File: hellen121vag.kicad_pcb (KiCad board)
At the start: 4 copper layers, 164 x 118 mm, 129 parts, among them J1 USB_B_Mini, J10 AudioJack_THR, J2 Conn_01x01, J3 Conn_01x01, J4 Conn_01x01, J5 Conn_01x01, J6 Conn_01x01, J7 Conn_01x08, J8 Conn_01x06, M1 Module-can-0.1, M10 Module-can-0.1, M11 Module-vr-discrete-0.1, M2 Module-power5-0.2, M3 Module-mcu-0.7, M4 Module-input-0.1, M5 Module-knock-0.1, M6 Module-output-0.3, M7 Module-ign8-0.2, M8 Module-power12-0.2, M9 Module-wbo-0.3, P1 368255-2, P10 Pad, P11 Pad, P12 Pad, P13 Pad, P14 Pad, P15 Pad, P16 Pad, P17 Pad, P2 Pad, P20 Pad, P28 Pad, P3 Pad, P4 Pad, P40 Pad, P41 Pad, P43 Pad, P44 Pad, P45 Pad, P46 Pad, P48 Pad, P49 Pad, P5 Pad, P56 Pad, P6 Pad, P61 Pad, P63 Pad, P64 Pad, P66 Pad, P67 Pad, P68 Pad, P69 Pad, P7 Pad, P74 Pad, P8 Pad, P80 Pad, P9 Pad, U1 L6205PD, U2 LPS25HB, U3 MCP6002-xSN, U4 TLS115_SOIC, U5 TLS115_SON

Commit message: Se agrego by avelito
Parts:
- moved U5 35.0 mm to (57.3, 68.4)
- moved C18 35.0 mm to (61.7, 69.0)
- moved C19 35.0 mm to (61.7, 67.1)
- moved U4 35.0 mm to (56.5, 62.8)
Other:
- board text added: "By Abelito"

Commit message: se modifico esquema y pcb
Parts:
- removed D10, D11, D12, D13, D14: B5819W, Diode_SMD:D_SOD-123
- removed D7, D8: LED-GREEN-0805, hellen-one-common:LED-0805
- removed D9: 1N4148WS, hellen-one-common:SOD-323
- removed G***, G6: LOGO, hellen-one-common:LOGO
- removed G3, G5: PROTO_AREA, hellen-one-common:PROTO_AREA
- removed G7: LOGO, rusefi_lib:LOGO
- removed J1: USB_B_Mini, hellen-one-common:USB-MINI-B-VERTICAL
- removed J10: AudioJack_THR, hellen-one-common:Jack_3.5mm_PJ-3250-5A
- removed J2, J3, J4, J5, J6: Conn_01x01, TestPoint:TestPoint_Pad_D2.0mm
- removed J7: Conn_01x08, Connector_PinHeader_2.54mm:PinHeader_1x08_P2.54mm_Vertical
- removed J8: Conn_01x06, Connector_PinHeader_2.54mm:PinHeader_1x06_P2.54mm_Vertical
- removed M10: Module-can-0.1, hellen-one-can-0.1:can
- removed M11: Module-vr-discrete-0.1, hellen-one-vr-discrete-0.1:vr-discrete
- removed M8: Module-power12-0.2, hellen-one-power12-0.2:power12
- removed M9: Module-wbo-0.3, hellen-one-wbo-0.3:wbo
- removed P14, P15, P16, P17, P20, P28, P40, P41, P43, P44, P45, P46, P48, P49, P56, P61, P63, P64, P66, P67, P68, P69, P74, P80: Pad, hellen-one-common:PAD-TH
- removed S1, S2: Button_SPST, hellen-one-common:SMD-2_2.9x3.9x1.7
- added C20: 10u, hellen-one-common:C0805, F.Cu at (159.9, 187.8)
- added C21: 10u, hellen-one-common:C0805, F.Cu at (159.9, 190.1)
- added C22: 10u, hellen-one-common:C0805, F.Cu at (159.9, 192.3)
- added C23: 10u, hellen-one-common:C0805, F.Cu at (159.9, 194.6)
- added C24: 10u, hellen-one-common:C0805, F.Cu at (159.9, 196.8)
- added C25: 100n, hellen-one-common:C0603, F.Cu at (217.2, 170.4)
- added C26: 10n, hellen-one-common:C0603, F.Cu at (220.7, 162.6)
- added C27: 10n, hellen-one-common:C0603, F.Cu at (220.7, 164.5)
- added C28: 100n, hellen-one-common:C0603, F.Cu at (220.7, 166.5)
- added C29: 10n, hellen-one-common:C0603, F.Cu at (220.7, 168.4)
- added C30: 100n, hellen-one-common:C0603, F.Cu at (220.7, 170.4)
- added C31: 10n, hellen-one-common:C0603, F.Cu at (224.1, 162.6)
- added C32: 100n, hellen-one-common:C0603, F.Cu at (224.1, 164.5)
- added C33: 1u, hellen-one-common:C0603, F.Cu at (224.1, 166.5)
- added F10: 50mA, Fuse:Fuse_0603_1608Metric, F.Cu at (217.9, 226.5)
- added F3: 12H1500D, hellen-one-common:PAD-1206-PAD, F.Cu at (219.9, 240.6)
- added F4: 12H1500D, hellen-one-common:PAD-1206-PAD, F.Cu at (219.9, 243.7)
- added F5: 50mA, Fuse:Fuse_0603_1608Metric, F.Cu at (217.9, 214.0)
- added F6: 50mA, Fuse:Fuse_0603_1608Metric, F.Cu at (217.9, 216.5)
- added F7: 50mA, Fuse:Fuse_0603_1608Metric, F.Cu at (217.9, 219.0)
- added F8: 50mA, Fuse:Fuse_0603_1608Metric, F.Cu at (217.9, 221.5)
- added F9: 50mA, Fuse:Fuse_0603_1608Metric, F.Cu at (217.9, 224.0)
- added H1: M3, MountingHole:MountingHole_3.2mm_M3_Pad_Via, F.Cu at (211.9, 216.7)
- added H2: M3, MountingHole:MountingHole_3.2mm_M3_Pad_Via, F.Cu at (211.9, 224.6)
- added H3: M3, MountingHole:MountingHole_3.2mm_M3_Pad_Via, F.Cu at (211.9, 232.6)
- added H4: M3, MountingHole:MountingHole_3.2mm_M3_Pad_Via, F.Cu at (211.9, 240.5)
- added J17: Conn_01x06, Connector_PinHeader_2.54mm:PinHeader_1x06_P2.54mm_Vertical, F.Cu at (222.2, 215.0)
- added J21: Conn_01x05_Male, Connector_Molex:Molex_SPOX_5267-05A_1x05_P2.50mm_Vertical, F.Cu at (149.4, 202.1)
- added J22: USB_B_Mini, hellen-one-common:USB-MINI-B-VERTICAL, F.Cu at (220.4, 189.2)
- added J23: USB_C, kicad6-libraries:USB_C, F.Cu at (219.8, 154.7)
- added L1: 470R@100MHz, Inductor_SMD:L_0603_1608Metric, F.Cu at (217.9, 229.0)
- added L2: 470R@100MHz, Inductor_SMD:L_0603_1608Metric, F.Cu at (217.9, 231.5)
- added Q1: ISL9V3040D3ST, Package_TO_SOT_SMD:TO-252-2, F.Cu at (168.9, 154.7)
- added Q2: ISL9V3040D3ST, Package_TO_SOT_SMD:TO-252-2, F.Cu at (177.1, 154.7)
- added Q3: ISL9V3040D3ST, Package_TO_SOT_SMD:TO-252-2, F.Cu at (185.3, 154.7)
- added Q4: ISL9V3040D3ST, Package_TO_SOT_SMD:TO-252-2, F.Cu at (193.5, 154.7)
- added Q5: ISL9V3040D3ST, Package_TO_SOT_SMD:TO-252-2, F.Cu at (201.7, 154.7)
- added Q6: ISL9V3040D3ST, Package_TO_SOT_SMD:TO-252-2, F.Cu at (209.9, 154.7)
- added R14: 5.6k, hellen-one-common:R0603, F.Cu at (174.8, 239.2)
- added R15: 4.7k, hellen-one-common:R0603, F.Cu at (178.1, 227.5)
- added R24: 4.7k, hellen-one-common:R0603, F.Cu at (181.4, 231.4)
- added R25: 4.7k, hellen-one-common:R0603, F.Cu at (181.4, 233.4)
- added R26: 4.7k, hellen-one-common:R0603, F.Cu at (181.4, 235.3)
- added R27: 4.7k, hellen-one-common:R0603, F.Cu at (181.4, 237.3)
- added R28: 4.7k, hellen-one-common:R0603, F.Cu at (181.4, 239.2)
- added R29: 22, hellen-one-common:R0603, F.Cu at (184.7, 227.5)
- added R30: 22, hellen-one-common:R0603, F.Cu at (184.7, 229.5)
- added R31: 22, hellen-one-common:R0603, F.Cu at (184.7, 231.4)
- added R32: 0, Resistor_SMD:R_2512_6332Metric, F.Cu at (133.8, 211.3)
- added R33: 0, Resistor_SMD:R_2512_6332Metric, F.Cu at (133.8, 216.2)
- added R34: 0, Resistor_SMD:R_2512_6332Metric, F.Cu at (133.8, 221.0)
- added R35: 22, hellen-one-common:R0603, F.Cu at (184.7, 233.4)
- added R36: 22, hellen-one-common:R0603, F.Cu at (184.7, 235.3)
- added R37: 22, hellen-one-common:R0603, F.Cu at (184.7, 237.3)
- added R38: 0, Resistor_SMD:R_2512_6332Metric, F.Cu at (133.8, 225.9)
- added R39: 0, Resistor_SMD:R_2512_6332Metric, F.Cu at (133.8, 230.8)
- added R40: 0, Resistor_SMD:R_2512_6332Metric, F.Cu at (133.8, 235.7)
- added U10: MPX4/MPXH6400_MAP, kicad6-libraries:MPX-4_MAP, F.Cu at (200.8, 170.6)
- added U11: MAX31855KASA, Package_SO:SOIC-8_3.9x4.9mm_P1.27mm, F.Cu at (169.0, 240.2)
- added U6: TLE9201SG, Package_SO:Infineon_PG-DSO-12-11, F.Cu at (144.8, 229.2)
- added U7: TLE9201SG, Package_SO:Infineon_PG-DSO-12-11, F.Cu at (144.8, 238.9)
- added U8: VNLD5160TR-E, Package_SO:SOIC-8_3.9x4.9mm_P1.27mm, F.Cu at (169.0, 227.0)
- added U9: VNLD5160TR-E, Package_SO:SOIC-8_3.9x4.9mm_P1.27mm, F.Cu at (169.0, 233.6)
- BT1: value BATTERY_CR2032 -> CR1220; footprint Battery:BatteryHolder_Keystone_1060_1x2032 -> kicad6-libraries:CR1220-2
- C10, C11, C7, C8, C9: footprint Capacitor_SMD:C_0805_2012Metric -> hellen-one-common:C0805
- C12: value 10u -> 100n; footprint Capacitor_SMD:C_0805_2012Metric -> hellen-one-common:C0603
- C13, C14: value 10u -> 10n; footprint Capacitor_SMD:C_0805_2012Metric -> hellen-one-common:C0603
- C15, C16, C2, C6: value 100n -> 10u; footprint hellen-one-common:C0603 -> hellen-one-common:C0805
- C17: footprint hellen-one-common:C0603 -> hellen-one-common:C0805
- C18, C19: value 1u -> 10u; footprint hellen-one-common:C0603 -> hellen-one-common:C0805
- C3: value 220n -> 10u; footprint hellen-one-common:C0603 -> hellen-one-common:C0805
- C4: value 10n -> 10u; footprint hellen-one-common:C0603 -> hellen-one-common:C0805
- C5: value 5.6n -> 10u; footprint hellen-one-common:C0603 -> hellen-one-common:C0805
- D1, D2, D3: value 1N4148WS -> B5819W; footprint hellen-one-common:SOD-323 -> hellen-one-common:SOD-123
- D4: value LED-GREEN-0805 -> B5819W; footprint hellen-one-common:LED-0805 -> hellen-one-common:SOD-123
- D6: value LED-GREEN-0805 -> NUP2105L; footprint hellen-one-common:LED-0805 -> Package_TO_SOT_SMD:SOT-23
- F1, F2: value Fuse-Pad-Pad -> 12H1500D
- M1: value Module-can-0.1 -> Module-power_12and5V-0.3; footprint hellen-one-can-0.1:can -> hellen-one-power_12and5V-0.3:power_12and5V
- M2: value Module-power5-0.2 -> Module-knock-0.2; footprint hellen-one-power5-0.2:power5 -> hellen-one-knock-0.2:knock
- M3: value Module-mcu-0.7 -> Module-vr-discrete-0.5; footprint hellen-one-mcu-0.7:mcu -> hellen-one-vr-discrete-0.5:vr-discrete
- M4: value Module-input-0.1 -> Module-vr-max9924-0.1; footprint hellen-one-input-0.1:input -> hellen-one-vr-max9924-0.1:vr-max9924
- M5: value Module-knock-0.1 -> Module-wbo-0.5; footprint hellen-one-knock-0.1:knock -> hellen-one-wbo-0.5:wbo
- M6: value Module-output-0.3 -> Module:mega-mcu100/0.3; footprint hellen-one-output-0.3:output -> hellen-one-mega-mcu100-0.3:mega-mcu100
- M7: value Module-ign8-0.2 -> Module-can-0.1; footprint hellen-one-ign8-0.2:ign8 -> hellen-one-can-0.1:can
- P1: footprint hellen121vag:368255-2 -> 368255-2:368255-2
- R1: value 100 -> 4.7k
- R10, R11, R12: value Jumper-Pad-Pad -> 10k; footprint hellen-one-common:PAD-0805-PAD -> hellen-one-common:R0805
- R13: value Jumper-Pad-Pad -> 5.6k; footprint hellen-one-common:PAD-0805-PAD -> hellen-one-common:R0603
- R16, R17: value 5.1k -> 4.7k
- R2: value Jumper-Pad-Pad -> 33k; footprint hellen-one-common:PAD-0805-PAD -> hellen-one-common:R0603
- R20: value 1.6k -> 4.7k
- R21: value 750 -> 4.7k
- R22: value 10k -> 4.7k
- R23: value 0 -> 4.7k
- R3: value Jumper-Pad-Pad -> 6.8k; footprint hellen-one-common:PAD-0805-PAD -> hellen-one-common:R0603
- R5: value 100k -> 0
- R6: value 2.7k -> 0
- R7: value 2.7k -> DNP; footprint hellen-one-common:R0603 -> hellen-one-common:R0805
- R8, R9: value Jumper-Pad-Pad -> DNP; footprint hellen-one-common:PAD-0805-PAD -> hellen-one-common:R0805
- U1: value L6205PD -> JDY-33; footprint hellen-one-common:SO20POWER -> kicad6-libraries:JDY-33
- U2: value LPS25HB -> VNLD5160TR-E; footprint Package_LGA:ST_HLGA-10_2.5x2.5mm_P0.6mm_LayoutBorder3x2y -> Package_SO:SOIC-8_3.9x4.9mm_P1.27mm
- U3: value MCP6002-xSN -> VNLD5160TR-E
- U4: value TLS115_SOIC -> VNLD5160TR-E; footprint kicad6-libraries:PG-DSO-8-43_VIA -> Package_SO:SOIC-8_3.9x4.9mm_P1.27mm
- U5: value TLS115_SON -> VNLD5160TR-E; footprint Package_SON:HVSON-8-1EP_3x3mm_P0.65mm_EP1.6x2.4mm -> Package_SO:SOIC-8_3.9x4.9mm_P1.27mm
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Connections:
- BT1 pad 1: Net-(BT1-Pad1) -> Net-(BT1-+)
- BT1 pad 2: GND -> PIN114
- C1 pad 1: GND -> PIN114
- C1 pad 2: +12V_RAW -> +3.3VA
- C10 pad 1: GND -> PIN114
- C10 pad 2: +12V_RAW -> /DC Driver 1/PWR
- C11 pad 1: GND -> PIN114
- C11 pad 2: +12V_RAW -> /DC Driver 1/PWR
- C12 pad 1: GND -> PIN114
- C12 pad 2: +12V_RAW -> /DC Driver 1/PWR
- C13 pad 1: GND -> PIN114
- C13 pad 2: +12V_RAW -> PIN2
- C14 pad 1: GND -> PIN114
- C14 pad 2: +12V_RAW -> PIN1
- C15 pad 1: GND -> PIN114
- C15 pad 2: +3V3 -> /DC Driver 2/PWR
- C16 pad 1: GND -> PIN114
- C16 pad 2: +5V -> /DC Driver 2/PWR
- C17 pad 1: Net-(C17-Pad1) -> PIN114
- C17 pad 2: Net-(C17-Pad2) -> /DC Driver 2/PWR
- C18 pad 1: GND -> PIN114
- C18 pad 2: +12V_PROT -> /DC Driver 2/PWR
- C19 pad 1: GND -> PIN114
- C19 pad 2: +5VP -> /DC Driver 2/PWR
- C2 pad 1: GND -> PIN114
- C2 pad 2: +12V_RAW -> /DC Driver 1/PWR
- C3 pad 1: Net-(C3-Pad1) -> PIN114
- C3 pad 2: +12V_RAW -> /DC Driver 1/PWR
- C4 pad 1: Net-(C4-Pad1) -> PIN114
- C4 pad 2: Net-(C4-Pad2) -> /DC Driver 1/PWR
- C5 pad 1: GND -> PIN114
- C5 pad 2: Net-(C5-Pad2) -> /DC Driver 1/PWR
- C6 pad 1: GND -> PIN114
- C6 pad 2: /NRESET -> /DC Driver 1/PWR
- C7 pad 1: GND -> PIN114
- C7 pad 2: +12V_RAW -> /DC Driver 1/PWR
- C8 pad 1: GND -> PIN114
- C8 pad 2: +12V_RAW -> /DC Driver 1/PWR
- C9 pad 1: GND -> PIN114
- C9 pad 2: +12V_RAW -> /DC Driver 1/PWR
- D1 pad 1: Net-(D1-Pad1) -> +12V_RAW
- D1 pad 2: +12V_RAW -> PIN14
- D2 pad 1: Net-(C3-Pad1) -> +12V_RAW
- D2 pad 2: Net-(D1-Pad1) -> PIN15
- D3 pad 1: /IN_VIGN -> +12V_RAW
- D3 pad 2: Net-(D3-Pad2) -> PIN16
- D4 pad 1: /IN_VIGN -> +12V_RAW
- D4 pad 2: Net-(D3-Pad2) -> PIN88
- D5 pad 1: +12V_RAW -> /VBAT
- D5 pad 2: Net-(D5-Pad2) -> Net-(BT1-+)
- D6 pad 1: +5V -> Net-(U11-T-)
- D6 pad 2: Net-(D6-Pad2) -> Net-(U11-T+)
- F1 pad 1: Net-(F1-Pad1) -> PIN108
- F1 pad 2: +12V_RAW -> PIN22
- F2 pad 1: Net-(F2-Pad1) -> PIN23
- G1 pad 1: Net-(G1-Pad1) -> PIN114
- G1 pad 10: Net-(G1-Pad10) -> +12V_RAW
- G1 pad 11: Net-(G1-Pad1) -> PIN114
- G1 pad 12: Net-(G1-Pad12) -> PIN114
- G1 pad 13: Net-(G1-Pad13) -> +3.3VA
- G1 pad 14: Net-(G1-Pad14) -> +5VA
- G1 pad 15: Net-(G1-Pad10) -> +12V_RAW
- G1 pad 2: Net-(G1-Pad12) -> PIN114
- G1 pad 3: Net-(G1-Pad13) -> +3.3VA
- G1 pad 4: Net-(G1-Pad14) -> +5VA
- G1 pad 5: Net-(G1-Pad10) -> +12V_RAW
- G1 pad 6: Net-(G1-Pad1) -> PIN114
- G1 pad 7: Net-(G1-Pad12) -> PIN114
- G1 pad 8: Net-(G1-Pad13) -> +3.3VA
- G1 pad 9: Net-(G1-Pad14) -> +5VA
- M1 pad E1: GND -> /VBAT
- M1 pad S1: /CAN- -> PIN114
- M1 pad V1: +5V -> PIN116
- M1 pad V2: /CAN_VIO -> PIN22
- M3 pad E1: unconnected-(M3-PadE1) -> /VR_DISCRETE_THR
- M3 pad E2: unconnected-(M3-PadE2) -> /VR_DISCRETE_A
- M3 pad E3: unconnected-(M3-PadE3) -> /VR_DISCRETE
- M3 pad E4: unconnected-(M3-PadE4) -> +5VA
- M3 pad W1: /IGN1 -> PIN18
- M3 pad W2: /IGN2 -> PIN17
- M4 pad E1: GND -> unconnected-(M4-NC-PadE1)
- M4 pad E2: +5V -> unconnected-(M4-NC-PadE2)
- M4 pad E3: unconnected-(M4-PadE3) -> /VR_MAX9924
- M4 pad E4: unconnected-(M4-PadE4) -> +5VA
- M5 pad E1: +5VA -> PIN105
- M5 pad E2: GND -> PIN96
- M5 pad E3: /IN_KNOCK1 -> PIN103
- M5 pad W1: /IN_KNOCK1_RAW -> +5VA
- M5 pad W2: /VREF2 -> unconnected-(M5-CAN_VIO-PadW2)
- M6 pad G: GND -> PIN114
- M6 pad S1: unconnected-(M6-PadS1) -> PIN89
- M6 pad S10: /OUT_FUEL_PUMP_RELAY -> PIN41
- M6 pad S11: +12V_RAW -> PIN40
- M6 pad S12: Net-(P8-Pad1) -> /INTERNAL_MAP
- M6 pad S13: /OUT_VVT1_1 -> PIN37
- M6 pad S14: /OUT_VVT1_1 -> PIN84
- M6 pad S15: /OUT_INJ6 -> /ADC3
- M6 pad S16: /OUT_INJ2 -> PIN85
- M6 pad S17: /OUT_INJ3 -> PIN42
- M6 pad S18: /OUT_INJ1 -> PIN38
- M6 pad S2: unconnected-(M6-PadS2) -> PIN113
- M6 pad S3: GND -> PIN113
- M6 pad S4: /OUT_VVT2_B2 -> PIN113
- M6 pad S5: /OUT_VVT2_B1 -> unconnected-(M6-VREF2-PadS5)
- M6 pad S6: /OUT_FUEL_CONSUM -> /IN_VMAIN
- M6 pad S7: /OUT_IDLE -> /IN_AUX3
- M6 pad S8: Net-(P6-Pad1) -> PIN91
- M6 pad S9: unconnected-(M6-PadS9) -> PIN113
- M6 pad W1: /OUT_VVT1_2 -> PIN113
- M6 pad W10: /OUT_INJ5 -> /IGN1
- M6 pad W11: /OUT_INJ8 -> PIN82
- M6 pad W12: /OUT_INJ7 -> PIN83
- M6 pad W13: /OUT_MAIN_RELAY -> unconnected-(M6-V33_REF-PadW13)
- M6 pad W14: +5V -> unconnected-(M6-V5A_SWITCHABLE-PadW14)
- M6 pad W2: /OUT_VVT1_2 -> +5VA
- M6 pad W3: /OUT_CHECK_ENGINE -> /LS_HOT2
- M6 pad W4: /OUT_WASTEGATE -> /LS_HOT1
- M6 pad W5: +12V_PROT -> /IGN6
- M6 pad W6: /OUT_TACH -> /IGN5
- M6 pad W7: /OUT_INJ4 -> /IGN4
- M6 pad W8: unconnected-(M6-PadW8) -> /IGN3
- M6 pad W9: Net-(P7-Pad1) -> /IGN2
- M7 pad S1: /OUT_IGN8 -> Net-(M7-CANL)
- M7 pad S2: /OUT_IGN7 -> Net-(M7-CANH)
- M7 pad V1: /IGN8 -> +5VA
- M7 pad V2: /IGN7 -> +3.3VA
- M7 pad V5: /IGN4 -> Net-(M6-SPI2_SCK_/_CAN2_TX_(PB13))
- M7 pad V6: /IGN3 -> Net-(M6-SPI2_CS_/_CAN2_RX_(PB12))
- P1 pad 1: GND -> PIN1
- P1 pad 10: Net-(P1-Pad10) -> PIN10
- P1 pad 100: unconnected-(P1-Pad100) -> PIN100
- P1 pad 101: /IN_MAP2 -> PIN101
- P1 pad 102: /OUT_IGN1 -> PIN102
- P1 pad 103: /OUT_IGN5 -> PIN103
- P1 pad 104: /OUT_WASTEGATE -> PIN104
- P1 pad 105: /OUT_IDLE -> PIN105
- P1 pad 106: /IN_KNOCK1_RAW -> PIN106
- P1 pad 107: unconnected-(P1-Pad107) -> PIN106
- P1 pad 108: GNDA -> PIN108
- P1 pad 109: unconnected-(P1-Pad109) -> PIN109
- P1 pad 11: Net-(P1-Pad11) -> PIN11
- P1 pad 110: /OUT_IGN6 -> PIN110
- P1 pad 111: /OUT_IGN3 -> PIN111
- P1 pad 112: /OUT_INJ6 -> PIN112
- P1 pad 113: /OUT_INJ5 -> PIN113
- P1 pad 114: unconnected-(P1-Pad114) -> PIN114
- P1 pad 115: /OUT_VVT1_2 -> PIN114
- P1 pad 116: unconnected-(P1-Pad116) -> PIN116
- P1 pad 117: /+ETB_OUT -> PIN117
- P1 pad 118: /-ETB_OUT -> PIN118
- P1 pad 119: unconnected-(P1-Pad119) -> PIN119
- P1 pad 12: Net-(P1-Pad12) -> PIN12
- P1 pad 120: /OUT_VVT2_B2 -> PIN120
- P1 pad 121: Net-(F2-Pad1) -> PIN121
- P1 pad 13: Net-(P1-Pad13) -> PIN13
- P1 pad 14: /IN_AFR -> PIN14
- P1 pad 15: unconnected-(P1-Pad15) -> PIN15
- P1 pad 16: unconnected-(P1-Pad16) -> PIN16
- P1 pad 17: Net-(P1-Pad17) -> PIN17
- P1 pad 18: /OUT_VVT2_B1 -> PIN18
- P1 pad 19: /OUT_INJ7 -> PIN19
- P1 pad 2: GND -> PIN2
- P1 pad 20: Net-(P1-Pad20) -> PIN20
- P1 pad 21: Net-(P1-Pad21) -> PIN21
- P1 pad 22: /OUT_VVT1_1 -> PIN22
- P1 pad 23: Net-(P1-Pad23) -> PIN23
- P1 pad 24: /OUT_INJ8 -> PIN23
- P1 pad 25: unconnected-(P1-Pad25) -> PIN25
- P1 pad 26: /IN_IAT -> PIN26
- P1 pad 27: GNDA -> PIN27
- P1 pad 28: Net-(P1-Pad28) -> PIN28
- P1 pad 29: /IN_MAF -> PIN29
- P1 pad 3: Net-(F1-Pad1) -> PIN114
- P1 pad 30: unconnected-(P1-Pad30) -> PIN30
- P1 pad 31: unconnected-(P1-Pad31) -> PIN31
- P1 pad 32: GND -> PIN32
- P1 pad 33: GNDA -> PIN33
- P1 pad 34: /IN_PPS1 -> PIN34
- P1 pad 35: /IN_PPS2 -> PIN35
- P1 pad 36: GNDA -> PIN36
- P1 pad 37: Net-(P1-Pad37) -> PIN37
- P1 pad 38: /IN_RES1 -> PIN38
- P1 pad 39: /IN_RES2 -> PIN39
- P1 pad 4: unconnected-(P1-Pad4) -> PIN4
- P1 pad 40: Net-(P1-Pad40) -> PIN40
- P1 pad 41: Net-(P1-Pad41) -> PIN41
- P1 pad 42: unconnected-(P1-Pad42) -> PIN42
- P1 pad 43: Net-(P1-Pad43) -> PIN43
- P1 pad 44: Net-(P1-Pad44) -> PIN44
- P1 pad 45: Net-(P1-Pad45) -> PIN45
- P1 pad 46: Net-(P1-Pad46) -> PIN46
- P1 pad 47: /OUT_CHECK_ENGINE -> PIN47
- P1 pad 48: Net-(P1-Pad48) -> PIN48
- P1 pad 49: Net-(P1-Pad49) -> PIN49
- P1 pad 5: /LSU_HEAT- -> PIN5
- P1 pad 50: GNDA -> PIN50
- P1 pad 51: Net-(P1-Pad51) -> PIN51
- P1 pad 52: Net-(P1-Pad52) -> PIN113
- P1 pad 53: +5VP -> PIN113
- P1 pad 54: /IN_VSS -> PIN113
- P1 pad 55: /IN_D1 -> PIN113
- P1 pad 56: Net-(P1-Pad56) -> PIN113
- P1 pad 57: /IN_D2 -> PIN113
- P1 pad 58: /CAN- -> PIN113
- P1 pad 59: GND -> PIN113
- P1 pad 6: unconnected-(P1-Pad6) -> PIN6
- P1 pad 60: /CAN+ -> PIN113
- P1 pad 61: Net-(P1-Pad61) -> PIN113
- P1 pad 62: /V12_PERM -> PIN113
- P1 pad 63: Net-(P1-Pad63) -> PIN63
- P1 pad 64: Net-(P1-Pad64) -> PIN113
- P1 pad 65: /OUT_FUEL_PUMP_RELAY -> PIN65
- P1 pad 66: Net-(P1-Pad66) -> PIN113
- P1 pad 67: Net-(P1-Pad67) -> PIN67
- P1 pad 68: Net-(P1-Pad68) -> PIN113
- P1 pad 69: Net-(P1-Pad69) -> PIN69
- P1 pad 7: /OUT_IGN2 -> PIN7
- P1 pad 70: Net-(P1-Pad70) -> PIN70
- P1 pad 71: Net-(P1-Pad71) -> PIN106
- P1 pad 72: +5VP -> PIN106
- P1 pad 73: +5VP -> PIN106
- P1 pad 74: Net-(P1-Pad74) -> PIN106
- P1 pad 75: /IN_D3 -> PIN106
- P1 pad 76: /IN_D4 -> PIN106
- P1 pad 77: unconnected-(P1-Pad77) -> PIN106
- P1 pad 78: unconnected-(P1-Pad78) -> PIN106
- P1 pad 79: unconnected-(P1-Pad79) -> PIN106
- P1 pad 8: /OUT_IGN7 -> PIN8
- P1 pad 80: Net-(P1-Pad80) -> PIN106
- P1 pad 81: /OUT_FUEL_CONSUM -> PIN81
- P1 pad 82: /IN_CRANK+ -> PIN82
- P1 pad 83: +5VP -> PIN83
- P1 pad 84: /IN_TPS2 -> PIN84
- P1 pad 85: /IN_IAT -> PIN85
- P1 pad 86: /IN_CAM1 -> PIN86
- P1 pad 87: /IN_CAM2 -> PIN87
- P1 pad 88: /OUT_INJ4 -> PIN88
- P1 pad 89: /OUT_INJ2 -> PIN89
- P1 pad 9: Net-(P1-Pad9) -> PIN9
- P1 pad 90: /IN_CRANK- -> PIN90
- P1 pad 91: GNDA -> PIN91
- P1 pad 92: /IN_TPS1 -> PIN92
- P1 pad 93: /IN_CLT -> PIN93
- P1 pad 94: /OUT_IGN4 -> PIN94
- P1 pad 95: /OUT_IGN8 -> PIN95
- P1 pad 96: /OUT_INJ1 -> PIN96
- P1 pad 97: /OUT_INJ3 -> PIN97
- P1 pad 98: +5VP -> PIN113
- P1 pad 99: GNDA -> PIN113
- P10 pad 1: Net-(P1-Pad10) -> /DC1_PWM
- P11 pad 1: Net-(P1-Pad11) -> /DC1_DIR
- P12 pad 1: Net-(P1-Pad12) -> /DC2_PWM
- P13 pad 1: Net-(P1-Pad13) -> /DC2_DIR
- P2 pad 1: /IN_A1 -> /VR_DISCRETE
- P3 pad 1: /IN_A4 -> /VR_MAX9924
- P4 pad 1: /IN_A2 -> Net-(M6-LED_GREEN)
- P5 pad 1: /IN_A3 -> Net-(M6-LED_YELLOW)
- P6 pad 1: Net-(P6-Pad1) -> Net-(M6-UART2_RX_(PD6))
- P7 pad 1: Net-(P7-Pad1) -> Net-(M6-UART2_TX_(PD5))
- P8 pad 1: Net-(P8-Pad1) -> Net-(M7-CANL)
- P9 pad 1: Net-(P1-Pad9) -> Net-(M7-CANH)
- R1 pad 1: Net-(D1-Pad1) -> PIN106
- R1 pad 2: Net-(C4-Pad2) -> PIN20
- R10 pad 1: Net-(P1-Pad51) -> PIN113
- R10 pad 2: /LSU_SENSOR_U/PUMP_I -> PIN84
- R11 pad 1: Net-(P1-Pad52) -> PIN113
- R11 pad 2: /LSU_PUMP_I -> PIN85
- R12 pad 1: Net-(P1-Pad70) -> PIN113
- R12 pad 2: /LSU_SENSOR_U -> PIN89
- R13 pad 1: Net-(P1-Pad71) -> PIN114
- R13 pad 2: /LSU_CALIBR_RES -> Net-(J23-CC1)
- R16 pad 1: Net-(D3-Pad2) -> PIN114
- R16 pad 2: GND -> /INJ4
- R17 pad 1: Net-(D5-Pad2) -> PIN114
- R17 pad 2: GND -> /INJ6
- R18 pad 1: +3V3 -> PIN114
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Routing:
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- added copper zone on B.Cu, net PIN113
- added copper zone on F.Cu, net PIN113
- removed copper zone on B.Cu, net /OUT_INJ2
- removed copper zone on B.Cu, net GND
- removed copper zone on F.Cu, net GND
- removed copper zone on In1.Cu, net GND
- removed copper zone on B.Cu, net Net-(J1-Pad5)
- removed copper zone on F.Cu, net Net-(J1-Pad5)
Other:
- outline, holes or cut-outs redrawn
- board text removed: "+12"
- board text removed: "+3.3"
- board text removed: "+5"
- board text removed: "1"
- board text removed: "10"
- board text removed: "100"
- board text removed: "101"
- board text removed: "102"
- board text removed: "103"
- board text removed: "104"
- board text removed: "105"
- board text removed: "106"
- board text removed: "11"
- board text removed: "112"
- board text removed: "113"
- board text removed: "114"
- board text removed: "115"
- board text removed: "116"
- board text removed: "117"
- board text removed: "118"
- board text removed: "119"
- board text removed: "12"
- board text removed: "120"
- board text removed: "121"
- board text removed: "12V SRC"
- board text removed: "13"
- board text removed: "14"
- board text removed: "15"
- board text removed: "16"
- board text removed: "17"
- board text removed: "18"
- board text removed: "19"
- board text removed: "2"
- board text removed: "20"
- board text removed: "21"
- board text removed: "22"
- board text removed: "23"
- board text removed: "24"
- board text removed: "25"
- board text removed: "26"
- board text removed: "27"
- board text removed: "28"
- board text removed: "29"
- board text removed: "3"
- board text removed: "3.3"
- board text removed: "30"
- board text removed: "31"
- board text removed: "32"
- board text removed: "33"
- board text removed: "34"
- board text removed: "35"
- board text removed: "36"
- board text removed: "37"
- board text removed: "38"
- board text removed: "39"
- board text removed: "4"
- board text removed: "40"
- board text removed: "41"
- board text removed: "42"
- board text removed: "43"
- board text removed: "44"
- board text removed: "45"
- board text removed: "46"
- board text removed: "47"
- board text removed: "48"
- board text removed: "49"
- board text removed: "5"
- board text removed: "50"
- board text removed: "51"
- board text removed: "52"
- board text removed: "53"
- board text removed: "54"
- board text removed: "55"
- board text removed: "56"
- board text removed: "57"
- board text removed: "58"
- board text removed: "59"
- board text removed: "6"
- board text removed: "60"
- board text removed: "61"
- board text removed: "62"
- board text removed: "63"
- board text removed: "64"
- board text removed: "65"
- board text removed: "66"
- board text removed: "67"
- board text removed: "68"
- board text removed: "69"
- board text removed: "7"
- board text removed: "70"
- board text removed: "71"
- board text removed: "72"
- board text removed: "73"
- board text removed: "74"
- board text removed: "75"
- board text removed: "76"
- board text removed: "77"
- board text removed: "78"
- board text removed: "79"
- board text removed: "8"
- board text removed: "80"
- board text removed: "81"
- board text removed: "82"
- board text removed: "83"
- board text removed: "84"
- board text removed: "85"
- board text removed: "86"
- board text removed: "87"
- board text removed: "88"
- board text removed: "89"
- board text removed: "9"
- board text removed: "90"
- board text removed: "91"
- board text removed: "92"
- board text removed: "93"
- board text removed: "94"
- board text removed: "95"
- board text removed: "96"
- board text removed: "97"
- board text removed: "98"
- board text removed: "99"
- board text removed: "<- Knock audio"
- board text removed: "Always looking for C/C++/PHP/Java developers https://rusefi.com/s/mission"
- board text removed: "Baro"
- board text removed: "By Abelito"
- board text removed: "CLK"
- board text removed: "DIO"
- board text removed: "G"
- board text removed: "GND"
- board text removed: "Hellen121vag"
- board text removed: "PROG"
- board text removed: "RESET"
- board text removed: "RST"
- board text removed: "SWD WBO"
- board text removed: "Vign"
- board text removed: "http://rusefi.com/s/hellen121vag"
- board text removed: "rev. d"
- board text removed: "© andreika, 2021"

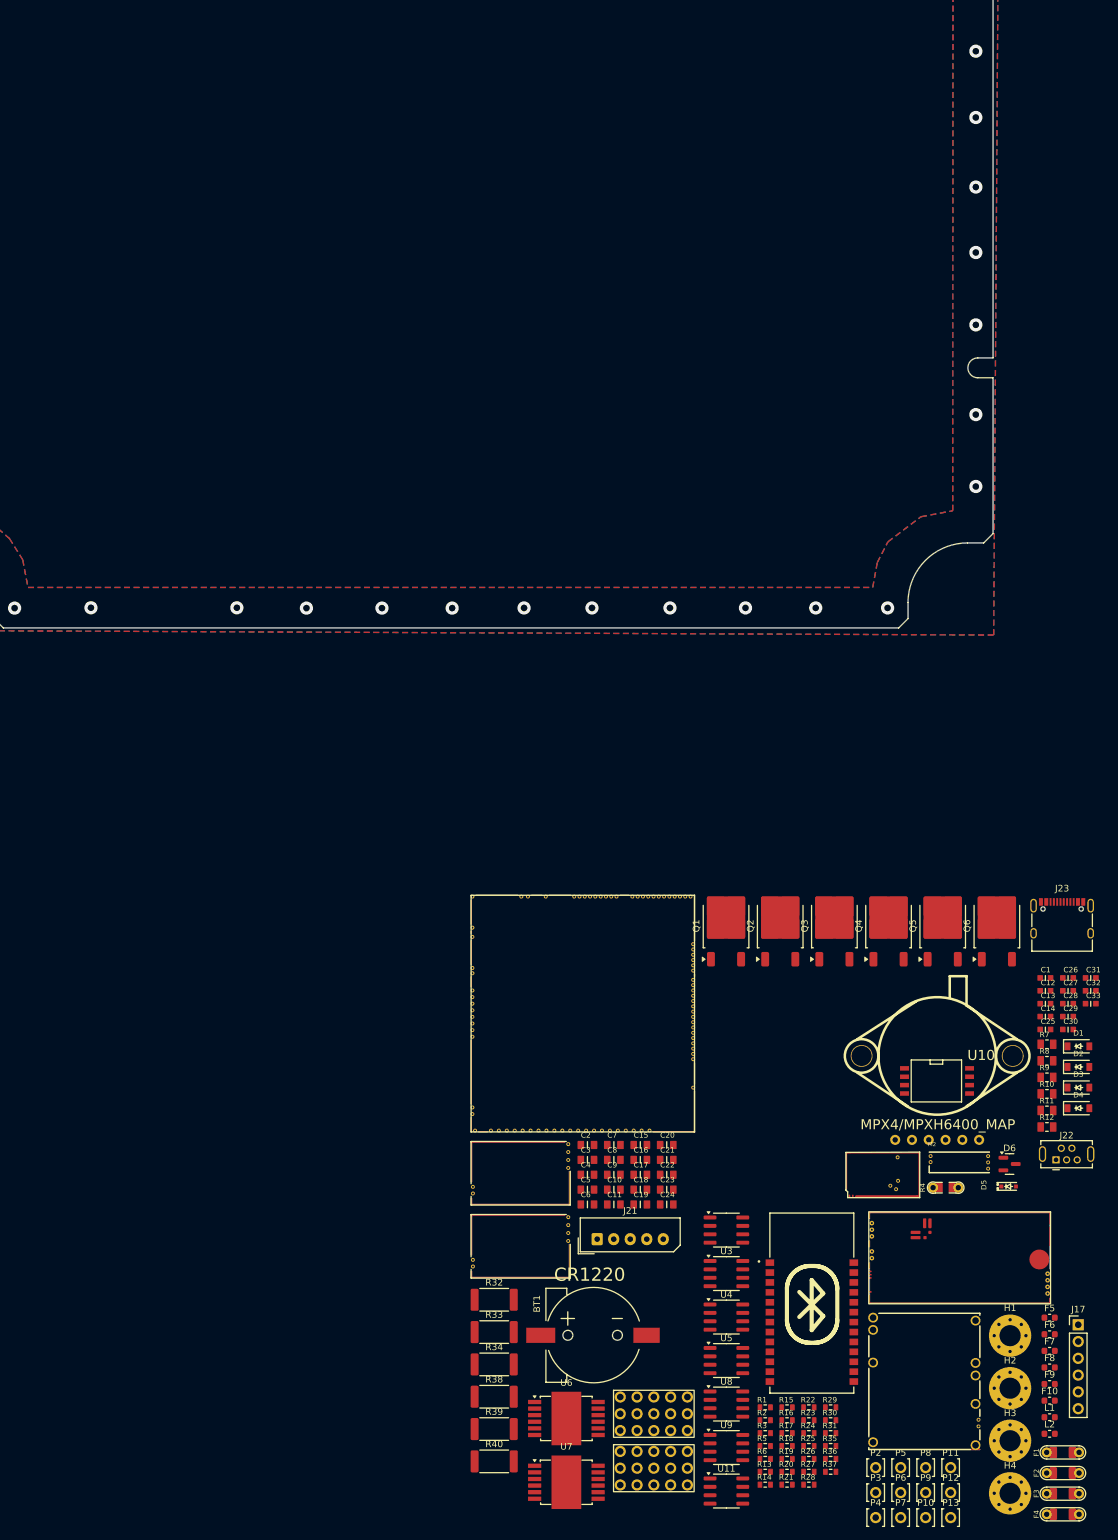
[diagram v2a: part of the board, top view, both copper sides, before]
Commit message: colocacion de los componentes en un 90%
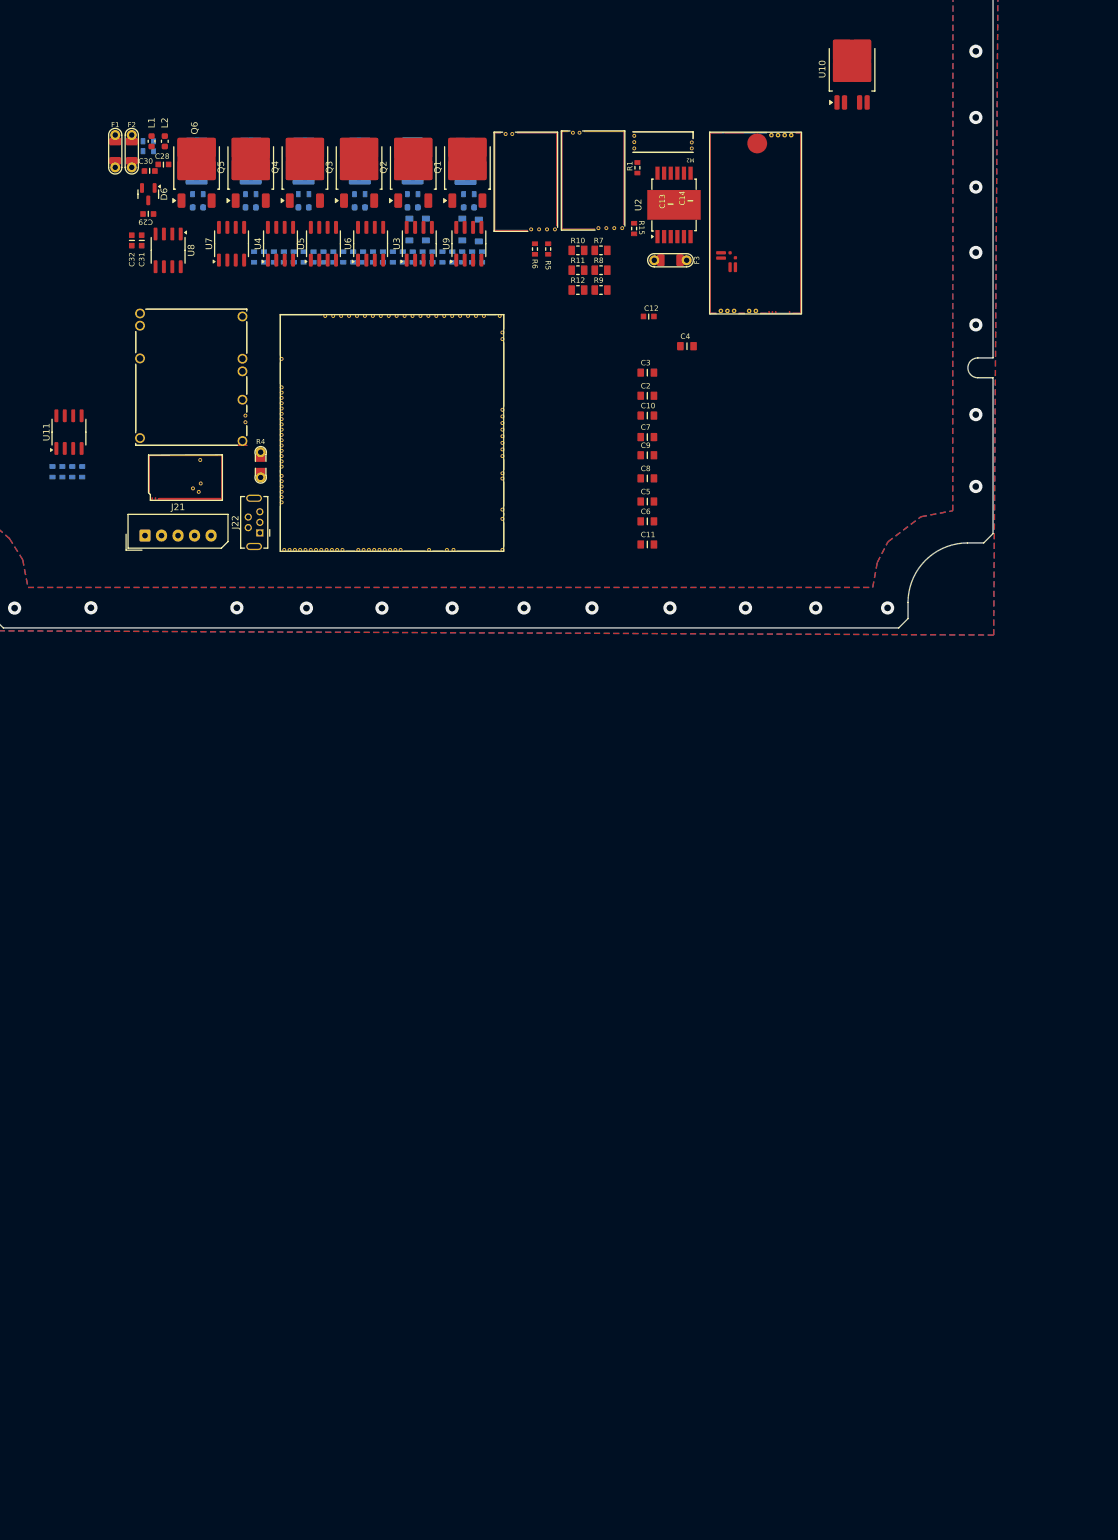
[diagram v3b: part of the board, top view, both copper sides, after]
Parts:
- removed BT1: CR1220, kicad6-libraries:CR1220-2
- removed C1, C25: 100n, hellen-one-common:C0603
- removed C15, C16, C17, C18, C19, C20, C21, C22, C23, C24: 10u, hellen-one-common:C0805
- removed C26, C27: 10n, hellen-one-common:C0603
- removed C33: 1u, hellen-one-common:C0603
- removed D5: 1N4148WS, hellen-one-common:SOD-323
- removed F4: 12H1500D, hellen-one-common:PAD-1206-PAD
- removed G1, G2: PROTO_AREA, hellen-one-common:PROTO_AREA
- removed G4: DISCLAIMER, rusefi_lib:Off_Road_Disclaimer
- removed H1, H2, H3, H4: M3, MountingHole:MountingHole_3.2mm_M3_Pad_Via
- removed J17: Conn_01x06, Connector_PinHeader_2.54mm:PinHeader_1x06_P2.54mm_Vertical
- removed J23: USB_C, kicad6-libraries:USB_C
- removed P10, P11, P12, P13, P2, P3, P4, P5, P6, P7, P8, P9: Pad, hellen-one-common:PAD-TH
- removed U1: JDY-33, kicad6-libraries:JDY-33
- added R41: 4.7k, hellen-one-common:R0603, B.Cu at (71.5, 86.0)
- added R42: 4.7k, hellen-one-common:R0603, B.Cu at (127.5, 53.5)
- added R43: 4.7k, hellen-one-common:R0603, B.Cu at (130.5, 53.5)
- added R44: 4.7k, hellen-one-common:R0603, B.Cu at (121.5, 53.5)
- added R45: 4.7k, hellen-one-common:R0603, B.Cu at (124.5, 53.5)
- added R46: 4.7k, hellen-one-common:R0603, B.Cu at (103.5, 53.5)
- added R47: 4.7k, hellen-one-common:R0603, B.Cu at (106.5, 53.5)
- added R48: 4.7k, hellen-one-common:R0603, B.Cu at (109.5, 53.5)
- added R49: 4.7k, hellen-one-common:R0603, B.Cu at (112.5, 53.5)
- added R50: 4.7k, hellen-one-common:R0603, B.Cu at (115.5, 53.5)
- added R51: 4.7k, hellen-one-common:R0603, B.Cu at (118.5, 53.5)
- added R52: 4.7k, hellen-one-common:R0603, B.Cu at (67.0, 86.0)
- added R53: 4.7k, hellen-one-common:R0603, B.Cu at (70.0, 86.0)
- C28, C30: value 100n -> 10n
- C29, C31: value 10n -> 100n
- C32: value 100n -> 1u
- D1, D2, D3, D4, F10, F5, F6, F7, F8, F9, R16, R2, R3: moved to B.Cu
- R13, R14: value 5.6k -> 4.7k; moved to B.Cu
- R17, R18, R19, R23, R24, R25: value 4.7k -> 22; moved to B.Cu
- R20, R21, R22, R26, R27, R28: value 4.7k -> 0; footprint hellen-one-common:R0603 -> Resistor_SMD:R_2512_6332Metric; moved to B.Cu
- R29, R30, R31, R35, R36, R37: value 22 -> 4.7k; moved to B.Cu
- R32, R33, R34, R38, R39, R40: value 0 -> 4.7k; footprint Resistor_SMD:R_2512_6332Metric -> hellen-one-common:R0603; moved to B.Cu
- U10: value MPX4/MPXH6400_MAP -> BTS6143D; footprint kicad6-libraries:MPX-4_MAP -> Package_TO_SOT_SMD:TO-252-4
- U11: value MAX31855KASA -> VNLD5160TR-E
- U2: value VNLD5160TR-E -> TLE9201SG; footprint Package_SO:SOIC-8_3.9x4.9mm_P1.27mm -> Package_SO:Infineon_PG-DSO-12-11
- U6, U7: value TLE9201SG -> VNLD5160TR-E; footprint Package_SO:Infineon_PG-DSO-12-11 -> Package_SO:SOIC-8_3.9x4.9mm_P1.27mm
- U8: value VNLD5160TR-E -> MAX31855KASA
- moved F2 244.6 mm to (79.0, 37.5), turned to -90 degrees
- moved F1 243.5 mm to (76.5, 37.5), turned to -90 degrees
- moved L2 237.0 mm to (84.0, 36.0), turned to -90 degrees
- moved L1 236.1 mm to (82.0, 36.0), turned to -90 degrees
- moved F10 221.8 mm to (89.0, 46.0), turned to 180 degrees
- moved R28 220.6 mm to (88.8, 39.0), turned to 90 degrees
- moved R27 215.5 mm to (97.0, 39.0), turned to 90 degrees
- moved R3 215.2 mm to (81.5, 37.5), turned to 180 degrees
- moved F9 215.2 mm to (97.0, 46.0), turned to 180 degrees
- moved R2 214.8 mm to (81.5, 36.0)
- moved R25 210.7 mm to (89.0, 44.0)
- moved R26 210.7 mm to (105.0, 39.0), turned to 90 degrees
- moved F8 208.7 mm to (105.0, 46.0), turned to 180 degrees
- moved R21 208.1 mm to (121.5, 39.0), turned to 90 degrees
- moved R24 205.6 mm to (97.0, 44.0)
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- renumbered Q6 to Q1, Q5 to Q2, Q4 to Q3, Q3 to Q4, Q2 to Q5, Q1 to Q6
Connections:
- net Net-(M6-SPI2_SCK_/_CAN2_TX_(PB13)) renamed E7INJ8CANTX
- C28 pad 2: +5VA -> Net-(U8-T-)
- C29 pad 1: PIN114 -> Net-(U8-T-)
- C29 pad 2: Net-(U11-T-) -> Net-(U8-T+)
- C30 pad 1: Net-(U11-T-) -> PIN114
- C30 pad 2: Net-(U11-T+) -> Net-(U8-T+)
- C31 pad 2: Net-(U11-T+) -> +3.3VA
- D6 pad 1: Net-(U11-T-) -> Net-(U8-T-)
- D6 pad 2: Net-(U11-T+) -> Net-(U8-T+)
- F1 pad 2: PIN22 -> /IN_VIGN
- F2 pad 1: PIN23 -> PIN120
- F3 pad 1: PIN23 -> PIN120
- L1 pad 2: Net-(U11-T+) -> Net-(U8-T+)
- L2 pad 2: Net-(U11-T-) -> Net-(U8-T-)
- M1 pad V2: PIN22 -> /IN_VIGN
- M5 pad W5: Net-(J17-Pin_5) -> unconnected-(M5-nReset-PadW5)
- M5 pad W6: Net-(J17-Pin_4) -> unconnected-(M5-SWDIO-PadW6)
- M5 pad W7: Net-(J17-Pin_2) -> unconnected-(M5-SWCLK-PadW7)
- M5 pad W8: Net-(J17-Pin_1) -> unconnected-(M5-V33_OUT-PadW8)
- M6 pad E6: Net-(M6-SPI2_CS_/_CAN2_RX_(PB12)) -> E6INJ7CANRX
- M6 pad N13: Net-(M6-UART2_TX_(PD5)) -> PIN7
- M6 pad N14: Net-(M6-UART2_RX_(PD6)) -> PIN6
- M6 pad N14a: Net-(M6-LED_GREEN) -> unconnected-(M6-LED_GREEN-PadN14a)
- M6 pad N14b: Net-(M6-LED_YELLOW) -> unconnected-(M6-LED_YELLOW-PadN14b)
- M7 pad S1: Net-(M7-CANL) -> unconnected-(M7-CANL-PadS1)
- M7 pad S2: Net-(M7-CANH) -> unconnected-(M7-CANH-PadS2)
- M7 pad V6: Net-(M6-SPI2_CS_/_CAN2_RX_(PB12)) -> E6INJ7CANRX
- P1 pad 23: PIN23 -> PIN120
- P1 pad 24: PIN23 -> PIN120
- Q1 pad 1: Net-(Q6-G) -> Net-(Q1-G)
- Q1 pad 2: PIN8 -> PIN13
- Q2 pad 1: Net-(Q5-G) -> Net-(Q2-G)
- Q2 pad 2: PIN11 -> PIN12
- Q3 pad 1: Net-(Q4-G) -> Net-(Q3-G)
- Q3 pad 2: PIN9 -> PIN10
- Q4 pad 1: Net-(Q3-G) -> Net-(Q4-G)
- Q4 pad 2: PIN10 -> PIN9
- Q5 pad 1: Net-(Q2-G) -> Net-(Q5-G)
- Q5 pad 2: PIN12 -> PIN11
- Q6 pad 1: Net-(Q1-G) -> Net-(Q6-G)
- Q6 pad 2: PIN13 -> PIN8
- R13 pad 1: PIN114 -> /LS_HOT2
- R13 pad 2: Net-(J23-CC1) -> Net-(U7-IN1)
- R14 pad 1: PIN114 -> /LS_HOT1
- R14 pad 2: Net-(J23-CC2) -> Net-(U7-IN2)
- R15 pad 1: PIN114 -> /DC1_DIS
- R15 pad 2: /INJ2 -> +3.3V
- R16 pad 1: PIN114 -> /LS1
- R16 pad 2: /INJ4 -> PIN114
- R17 pad 1: PIN114 -> Net-(Q1-G)
- R17 pad 2: /INJ6 -> Net-(F5-Pad1)
- R18 pad 1: PIN114 -> Net-(Q2-G)
- R18 pad 2: /INJ1 -> Net-(F6-Pad1)
- R19 pad 1: PIN114 -> Net-(Q3-G)
- R19 pad 2: /INJ3 -> Net-(F7-Pad1)
- R2 pad 2: PIN23 -> PIN120
- R20 pad 1: PIN114 -> Net-(F5-Pad1)
- R20 pad 2: /INJ5 -> PIN13
- R21 pad 1: /LS_HOT1 -> Net-(F6-Pad1)
- R21 pad 2: PIN114 -> PIN12
- R22 pad 1: /LS_HOT2 -> Net-(F7-Pad1)
- R22 pad 2: PIN114 -> PIN10
- R23 pad 1: /DC1_DIS -> Net-(Q4-G)
- R23 pad 2: +3.3V -> Net-(F8-Pad1)
- R24 pad 1: /DC2_DIS -> Net-(Q5-G)
- R24 pad 2: +3.3V -> Net-(F9-Pad1)
- R25 pad 1: PIN114 -> Net-(Q6-G)
- R25 pad 2: /LS2 -> Net-(F10-Pad1)
- R26 pad 1: PIN114 -> Net-(F8-Pad1)
- R26 pad 2: /LS4 -> PIN9
- R27 pad 1: PIN114 -> Net-(F9-Pad1)
- R27 pad 2: /LS1 -> PIN11
- R28 pad 1: PIN114 -> Net-(F10-Pad1)
- R28 pad 2: /LS3 -> PIN8
- R29 pad 1: Net-(Q1-G) -> /INJ1
- R29 pad 2: Net-(F5-Pad1) -> PIN114
- R30 pad 1: Net-(Q2-G) -> /INJ3
- R30 pad 2: Net-(F6-Pad1) -> PIN114
- R31 pad 1: Net-(Q3-G) -> /INJ5
- R31 pad 2: Net-(F7-Pad1) -> PIN114
- R32 pad 1: Net-(F5-Pad1) -> /INJ2
- R32 pad 2: PIN13 -> PIN114
- R33 pad 1: Net-(F6-Pad1) -> /INJ4
- R33 pad 2: PIN12 -> PIN114
- R34 pad 1: Net-(F7-Pad1) -> /INJ6
- R34 pad 2: PIN10 -> PIN114
- R35 pad 1: Net-(Q4-G) -> /LS_HOT1
- R35 pad 2: Net-(F8-Pad1) -> PIN114
- R36 pad 1: Net-(Q5-G) -> /LS_HOT2
- R36 pad 2: Net-(F9-Pad1) -> PIN114
- R37 pad 1: Net-(Q6-G) -> /LS3
- R37 pad 2: Net-(F10-Pad1) -> PIN114
- R38 pad 1: Net-(F8-Pad1) -> /LS2
- R38 pad 2: PIN9 -> PIN114
- R39 pad 1: Net-(F9-Pad1) -> /LS4
- R39 pad 2: PIN11 -> PIN114
- R40 pad 1: Net-(F10-Pad1) -> E6INJ7CANRX
- R40 pad 2: PIN8 -> PIN114
- U10 pad 1: /INTERNAL_MAP -> Net-(U10-OUT-Pad1)
- U10 pad 2: PIN114 -> unconnected-(U10-IN-Pad2)
- U10 pad 3: +5VA -> unconnected-(U10-Vbb-Pad3)
- U10 pad 5: unconnected-(U10-V2-Pad5) -> Net-(U10-OUT-Pad1)
- U11 pad 1: PIN114 -> Net-(U11-IN1)
- U11 pad 2: Net-(U11-T-) -> unconnected-(U11-STATUS1-Pad2)
- U11 pad 3: Net-(U11-T+) -> Net-(U11-IN2)
- U11 pad 4: +3.3VA -> unconnected-(U11-STATUS2-Pad4)
- U11 pad 5: /SCK3 -> PIN114
- U11 pad 6: /EGT/SPI_CS -> PIN51
- U11 pad 7: /MISO3 -> PIN114
- U11 pad 8: (no net) -> PIN50
- U2 pad 1: /INJ1 -> /DC1_DIR
- U2 pad 2: unconnected-(U2-STATUS1-Pad2) -> +3.3V
- U2 pad 3: /INJ2 -> unconnected-(U2-SO-Pad3)
- U2 pad 4: unconnected-(U2-STATUS2-Pad4) -> /DC Driver 1/PWR
- U2 pad 5: PIN114 -> PIN2
- U2 pad 6: PIN45 -> PIN114
- U2 pad 7: PIN114 -> PIN1
- U2 pad 8: PIN44 -> PIN114
- U3 pad 1: /INJ3 -> Net-(U3-IN1)
- U3 pad 3: /INJ4 -> Net-(U3-IN2)
- U3 pad 6: PIN47 -> PIN15
- U3 pad 8: PIN46 -> PIN14
- U4 pad 1: /INJ5 -> Net-(U4-IN1)
- U4 pad 3: /INJ6 -> Net-(U4-IN2)
- U4 pad 6: PIN49 -> PIN45
- U4 pad 8: PIN48 -> PIN44
- U5 pad 1: /LS_HOT2 -> Net-(U5-IN1)
- U5 pad 3: /LS_HOT1 -> Net-(U5-IN2)
- U5 pad 6: /OUT_LS_HOT1 -> PIN47
- U5 pad 8: /OUT_LS_HOT2 -> PIN46
- U6 pad 1: /DC1_DIR -> Net-(U6-IN1)
- U6 pad 2: +3.3V -> unconnected-(U6-STATUS1-Pad2)
- U6 pad 3: unconnected-(U6-SO-Pad3) -> Net-(U6-IN2)
- U6 pad 4: /DC Driver 1/PWR -> unconnected-(U6-STATUS2-Pad4)
- U6 pad 5: PIN2 -> PIN114
- U6 pad 6: PIN114 -> PIN49
- U6 pad 7: PIN1 -> PIN114
- U6 pad 8: PIN114 -> PIN48
- U7 pad 1: /DC2_DIR -> Net-(U7-IN1)
- U7 pad 2: +3.3V -> unconnected-(U7-STATUS1-Pad2)
- U7 pad 3: unconnected-(U7-SO-Pad3) -> Net-(U7-IN2)
- U7 pad 4: /DC Driver 2/PWR -> unconnected-(U7-STATUS2-Pad4)
- U7 pad 5: PIN5 -> PIN114
- U7 pad 6: PIN114 -> PIN86
- U7 pad 7: PIN4 -> PIN114
- U7 pad 8: PIN114 -> PIN87
- U8 pad 1: /LS1 -> PIN114
- U8 pad 2: unconnected-(U8-STATUS1-Pad2) -> Net-(U8-T-)
- U8 pad 3: /LS2 -> Net-(U8-T+)
- U8 pad 4: unconnected-(U8-STATUS2-Pad4) -> +3.3VA
- U8 pad 5: PIN114 -> /SCK3
- U8 pad 6: PIN15 -> /EGT/SPI_CS
- U8 pad 7: PIN114 -> /MISO3
- U8 pad 8: PIN14 -> (no net)
- U9 pad 1: /LS3 -> Net-(U9-IN1)
- U9 pad 3: /LS4 -> Net-(U9-IN2)

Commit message: se ha completado un 99% la colocacion de componentes y adapatacion
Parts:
- removed C10, C11, C2, C3, C4, C5, C6, C7, C8, C9: 10u, hellen-one-common:C0805
- removed C12: 100n, hellen-one-common:C0603
- removed C13, C14: 10n, hellen-one-common:C0603
- removed R15: 4.7k, hellen-one-common:R0603
- removed U2: TLE9201SG, Package_SO:Infineon_PG-DSO-12-11
- added M8: Module-motor-driver-0.1, hellen-one-motor-driver-0.1:motor-driver, F.Cu at (166.9, 53.8)
- moved F3 5.10 mm to (161.5, 59.0)
- moved M5 2.06 mm to (182.4, 61.7)
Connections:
- F3 pad 2: /DC Driver 1/PWR -> Net-(F3-Pad2)
- M6 pad E8: /DC1_DIS -> DC1_DIS_W1
